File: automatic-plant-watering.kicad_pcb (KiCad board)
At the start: 4 copper layers, 61.5 x 42.2 mm, 53 parts, among them J1 Power, J2 USB_B_Mini, J3 MOTOR, J4 INPUT, J5 Power, Q1 BC847, Q2 BC847, Q3 TEPT4400, SW1 SW_Push, U1 ESP32-WROOM-32D, U2 TPS62132, U3 USBLC6-2SC6, U4 DHT11, U5 DRV8833PW, U6 CP2104

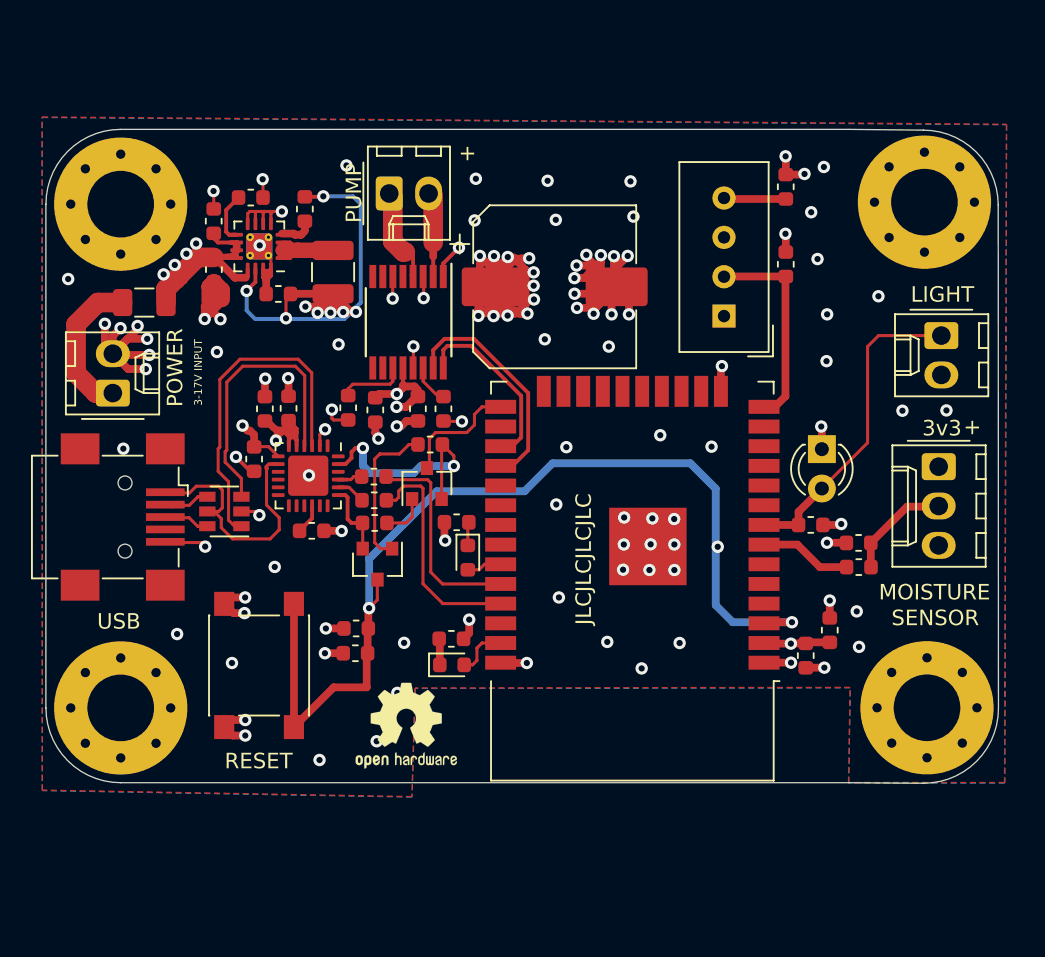
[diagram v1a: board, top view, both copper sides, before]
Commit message: added 3d model
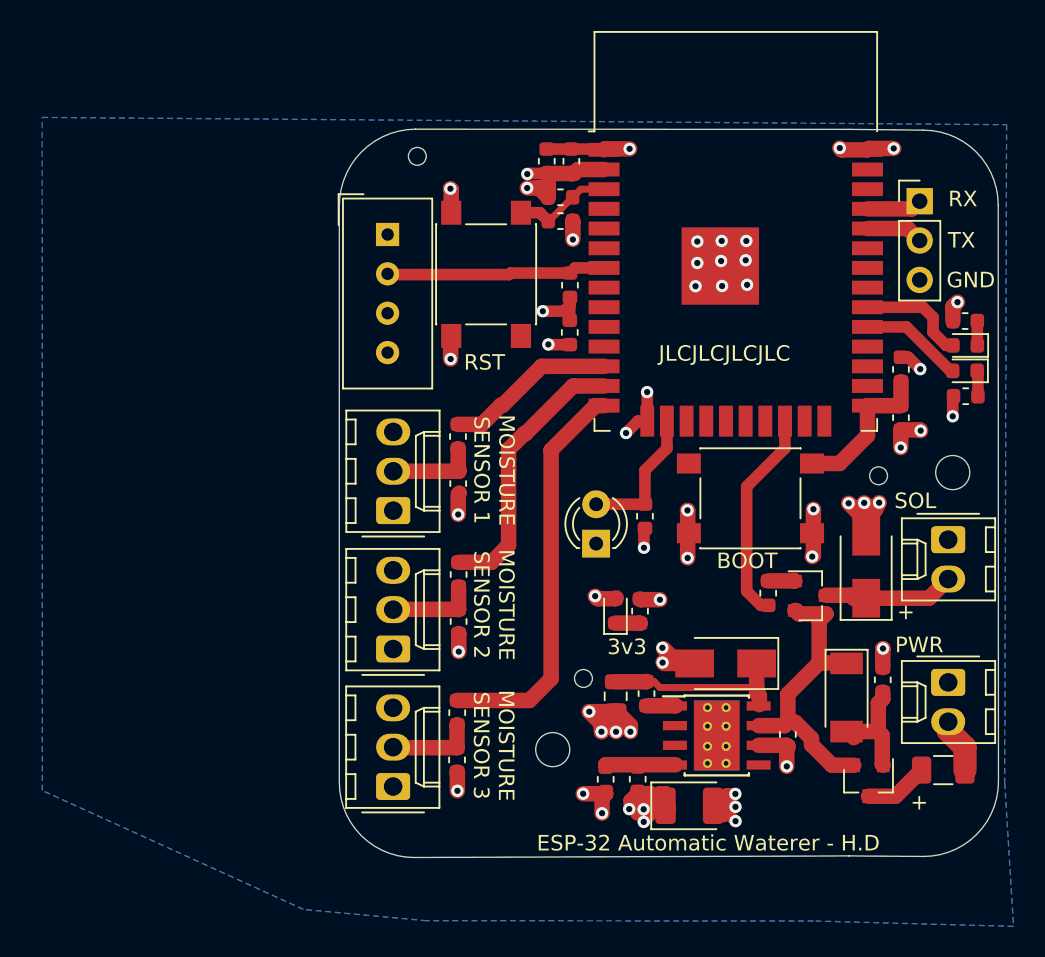
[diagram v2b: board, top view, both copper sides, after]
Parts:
- removed C11, C13, C21: 100n, Capacitor_SMD:C_0603_1608Metric
- removed C14: 2.2u, Capacitor_SMD:C_0603_1608Metric
- removed C15: 1u, Capacitor_SMD:C_0603_1608Metric
- removed C16: 10u, Capacitor_SMD:C_0603_1608Metric
- removed C17: 1000u, Capacitor_SMD:CP_Elec_10x10
- removed C18: 10n, Capacitor_SMD:C_0603_1608Metric
- removed C19: 4.7u, Capacitor_SMD:C_0603_1608Metric
- removed H2: TL, MountingHole:MountingHole_4.3mm_M4_Pad_Via
- removed H3: BR, MountingHole:MountingHole_4.3mm_M4_Pad_Via
- removed J5: Power, Connector_Molex:Molex_KK-254_AE-6410-02A_1x02_P2.54mm_Vertical
- removed R8: 10k, Resistor_SMD:R_0603_1608Metric
- removed REF**: OSHW-Logo2_7.3x6mm_SilkScreen, Symbol:OSHW-Logo2_7.3x6mm_SilkScreen
- removed U3: USBLC6-2SC6, Package_TO_SOT_SMD:SOT-23-6
- removed U5: DRV8833PW, Package_SO:TSSOP-16_4.4x5mm_P0.65mm
- removed U6: CP2104, Package_DFN_QFN:QFN-24-1EP_4x4mm_P0.5mm_EP2.6x2.6mm
- added C8: 100n, Capacitor_SMD:C_0603_1608Metric, F.Cu at (236.4, 122.7)
- added C9: 100n, Capacitor_SMD:C_0603_1608Metric, F.Cu at (236.4, 131.6)
- added D3: D_Zener, Diode_SMD:D_SOD-128, F.Cu at (261.5, 136.5)
- added D4: B340, Diode_SMD:D_SMA, F.Cu at (253.7, 134.3)
- added D5: D_Small, Diode_SMD:D_SMA, F.Cu at (262.7, 128.1)
- added D6: RED, LED_SMD:LED_0603_1608Metric, F.Cu at (246.6, 130.9)
- added J8: INPUT, Connector_Molex:Molex_KK-254_AE-6410-03A_1x03_P2.54mm_Vertical, F.Cu at (232.2, 133.4)
- added J9: INPUT, Connector_Molex:Molex_KK-254_AE-6410-03A_1x03_P2.54mm_Vertical, F.Cu at (232.2, 142.2)
- added R12: 10k, Resistor_SMD:R_0603_1608Metric, F.Cu at (248.0, 141.8)
- added R13: 5.6k, Resistor_SMD:R_0603_1608Metric, F.Cu at (245.9, 141.8)
- added R14: 10k, Resistor_SMD:R_0603_1608Metric, F.Cu at (236.4, 128.5)
- added R15: 10k, Resistor_SMD:R_0603_1608Metric, F.Cu at (236.3, 137.5)
- added SW2: SW_Push, Button_Switch_SMD:SW_Push_1P1T_NO_6x6mm_H9.5mm, F.Cu at (255.3, 123.6)
- C3: value 3.3nF -> 10u
- C4: value 22u -> 10n
- C6: value 10u -> 100u; footprint Capacitor_SMD:C_0603_1608Metric -> Capacitor_Tantalum_SMD:CP_EIA-3528-21_Kemet-B
- C7: value 0.1u -> 10u
- H1, H4: footprint MountingHole:MountingHole_4.3mm_M4_Pad_Via -> MountingHole:MountingHole_2.2mm_M2_DIN965
- J2: value USB_B_Mini -> PROG; footprint Connector_USB:USB_Mini-B_Wuerth_65100516121_Horizontal -> Connector_PinHeader_2.54mm:PinHeader_1x03_P2.54mm_Vertical
- J3: value MOTOR -> Power
- L1: value 2.2u -> L_Small; footprint Inductor_SMD:L_1210_3225Metric -> Inductor_SMD:L_0805_2012Metric
- Q1, Q2: value BC847 -> AO3401A
- R2: value 100k -> 10k
- R3, R4: value 0 -> 10k
- R5: value 10k -> 220
- U2: value TPS62132 -> TPS5430DDA; footprint Package_DFN_QFN:VQFN-16-1EP_3x3mm_P0.5mm_EP1.68x1.68mm_ThermalVias -> Package_SO:TI_SO-PowerPAD-8_ThermalVias
- moved F1 59.7 mm to (267.7, 141.2), turned to 0 degrees
- moved J1 57.1 mm to (268.0, 135.5), turned to 270 degrees
- moved J2 55.2 mm to (266.2, 104.5), turned to 0 degrees
- moved C3 49.0 mm to (257.7, 138.9), turned to 270 degrees
- moved R2 48.1 mm to (263.8, 135.3)
- moved C6 46.2 mm to (251.3, 143.5), turned to 0 degrees
- moved C7 45.4 mm to (265.0, 115.3)
- moved U2 43.2 mm to (253.1, 138.9), turned to 0 degrees
- moved J3 42.4 mm to (268.0, 126.3), turned to 270 degrees
- moved D2 39.0 mm to (269.1, 113.8), turned to 180 degrees
- moved R7 39.0 mm to (269.1, 112.2), turned to 0 degrees
- moved C1 35.3 mm to (242.1, 101.9)
- moved J4 35.3 mm to (232.2, 124.4), turned to 90 degrees
- moved C2 35.3 mm to (243.7, 101.9), turned to 90 degrees
- moved C4 35.1 mm to (248.6, 136.2), turned to 270 degrees
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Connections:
- C10 pad 1: +3V3 -> Net-(C10-Pad1)
- C3 pad 1: Net-(C3-Pad1) -> 12V_IN
- C4 pad 1: +3V3 -> Net-(C4-Pad1)
- C4 pad 2: GND -> Net-(C4-Pad2)
- C6 pad 1: Net-(C6-Pad1) -> +3V3
- C7 pad 1: Net-(C6-Pad1) -> GPIO0
- F1 pad 1: Net-(C6-Pad1) -> Net-(F1-Pad1)
- J1 pad 1: Net-(F1-Pad2) -> GND
- J1 pad 2: GND -> Net-(F1-Pad2)
- J2 pad 1: +5V -> RX_PROG
- J2 pad 2: USB_D- -> TX_PROG
- J2 pad 3: USB_D+ -> GND
- J3 pad 1: MOTOR1_NEGATIVE -> GND
- J3 pad 2: MOTOR1_POSITIVE -> Net-(D5-Pad1)
- L1 pad 1: Net-(L1-Pad1) -> Net-(C4-Pad1)
- Q1 pad 1: Net-(Q1-Pad1) -> Net-(D3-Pad2)
- Q1 pad 2: DTR -> 12V_IN
- Q1 pad 3: GPIO0 -> Net-(F1-Pad1)
- Q2 pad 2: RTS -> 12V_IN
- Q2 pad 3: RESET -> Net-(D5-Pad1)
- R10 pad 1: MOISTURE_SENSOR -> MOIST3
- R2 pad 1: Net-(R2-Pad1) -> Net-(D3-Pad2)
- R2 pad 2: +3V3 -> GND
- R3 pad 1: RX_CP -> +3V3
- R3 pad 2: Net-(R3-Pad2) -> GPIO0
- R4 pad 1: TX_CP -> Net-(Q2-Pad1)
- R4 pad 2: Net-(R4-Pad2) -> DRIVER
- R5 pad 1: Net-(Q1-Pad1) -> GND
- R5 pad 2: RTS -> Net-(D6-Pad1)
- U1 pad 12: Net-(U1-Pad12) -> MOIST3
- U1 pad 13: Net-(U1-Pad13) -> MOIST2
- U1 pad 14: TEMP_HUMID_SEN -> MOIST1
- U1 pad 16: Net-(U1-Pad16) -> LIGHT_SENSOR
- U1 pad 22: Net-(U1-Pad22) -> DRIVER
- U1 pad 27: IN1 -> Net-(U1-Pad27)
- U1 pad 28: IN2 -> Net-(U1-Pad28)
- U1 pad 29: Net-(U1-Pad29) -> Net-(D1-Pad2)
- U1 pad 30: Net-(U1-Pad30) -> Net-(D2-Pad2)
- U1 pad 33: Net-(D1-Pad2) -> Net-(U1-Pad33)
- U1 pad 34: Net-(R4-Pad2) -> TX_PROG
- U1 pad 35: Net-(R3-Pad2) -> RX_PROG
- U1 pad 37: Net-(D2-Pad2) -> Net-(U1-Pad37)
- U1 pad 7: MOISTURE_SENSOR -> TEMP_HUMID_SEN
- U1 pad 8: LIGHT_SENSOR -> Net-(U1-Pad8)
- U2 pad 1: Net-(L1-Pad1) -> Net-(C4-Pad2)
- U2 pad 2: Net-(L1-Pad1) -> Net-(U2-Pad2)
- U2 pad 3: Net-(L1-Pad1) -> Net-(U2-Pad3)
- U2 pad 4: Net-(R2-Pad1) -> Net-(R12-Pad2)
- U2 pad 5: GND -> Net-(U2-Pad5)
- U2 pad 7: GND -> 12V_IN
- U2 pad 8: GND -> Net-(C4-Pad1)
- U2 pad 9: Net-(C3-Pad1) -> GND
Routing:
- net +3V3: track 123.1 -> 36.5 mm, vias 31 -> 13
- net RESET: track 64.3 -> 6.44 mm, vias 3 -> 0
- net GND: track 110.1 -> 57.5 mm, vias 98 -> 42
- net MOIST1: track 0.00 -> 26.0 mm
- net Net-(C6-Pad1): track 23.9 -> 0.00 mm, vias 4 -> 0
- net D+: track 21.9 -> 0.00 mm
- net 12V_IN: track 0.00 -> 19.5 mm
- net D-: track 18.1 -> 0.00 mm
- net MOIST2: track 0.00 -> 17.7 mm
- net +5V: track 17.3 -> 0.00 mm
- net IN2: track 14.9 -> 0.00 mm
- net DTR: track 14.9 -> 0.00 mm, vias 2 -> 0
- net Net-(R3-Pad2): track 14.7 -> 0.00 mm
- net DRIVER: track 0.00 -> 13.8 mm
- net Net-(R4-Pad2): track 13.6 -> 0.00 mm
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- removed copper zone on F.Cu, net GND
- removed copper zone on POWER, net Net-(C6-Pad1)
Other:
- board size 61.5 x 42.2 mm -> 42.5 x 47 mm
- board text added: "BOOT"
- board text added: "ESP-32 Automatic Waterer - H.D"
- board text added: "GND"
- board text added: "MOISTURE SENSOR 1"
- board text added: "MOISTURE SENSOR 2"
- board text added: "MOISTURE SENSOR 3"
- board text added: "PWR"
- board text added: "RST"
- board text added: "RX"
- board text added: "SOL"
- board text added: "TX"
- board text removed: "3-17V INPUT"
- board text removed: "Designed By: Harry Dobbs (2021)"
- board text removed: "LIGHT"
- board text removed: "MOISTURE"
- board text removed: "POWER"
- board text removed: "PUMP"
- board text removed: "RESET"
- board text removed: "SENSOR"
- board text removed: "USB"

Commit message: fixed up some mistakes
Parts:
- moved R5 1.88 mm to (246.3, 130.7), turned to 90 degrees
- moved D6 1.32 mm to (247.9, 130.7), turned to 270 degrees
